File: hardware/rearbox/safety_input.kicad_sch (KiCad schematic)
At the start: 9 parts, among them U9 TLP291-4

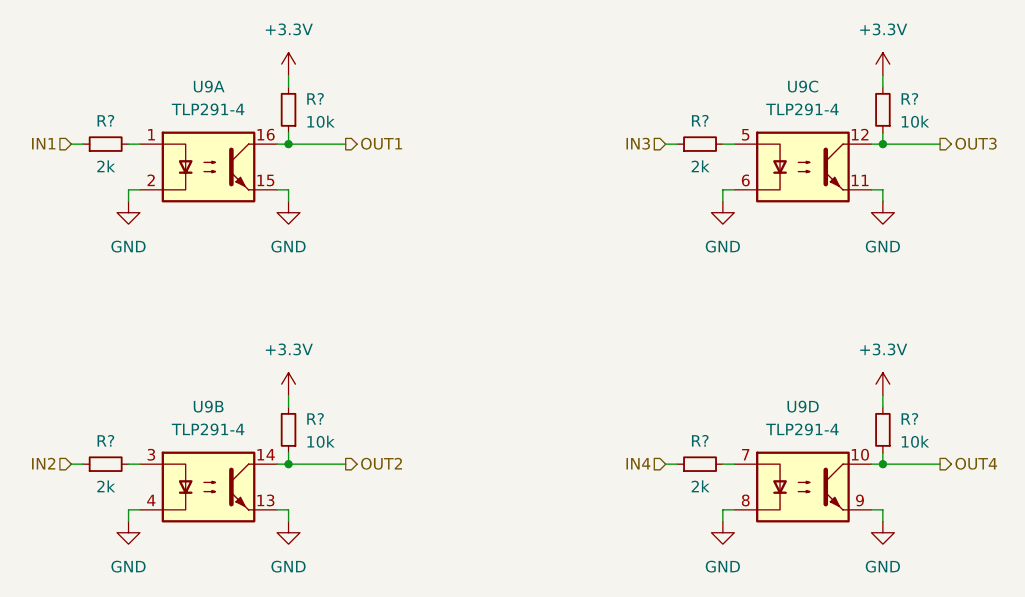
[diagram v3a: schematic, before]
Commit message: Route the tracks on the connector PCB
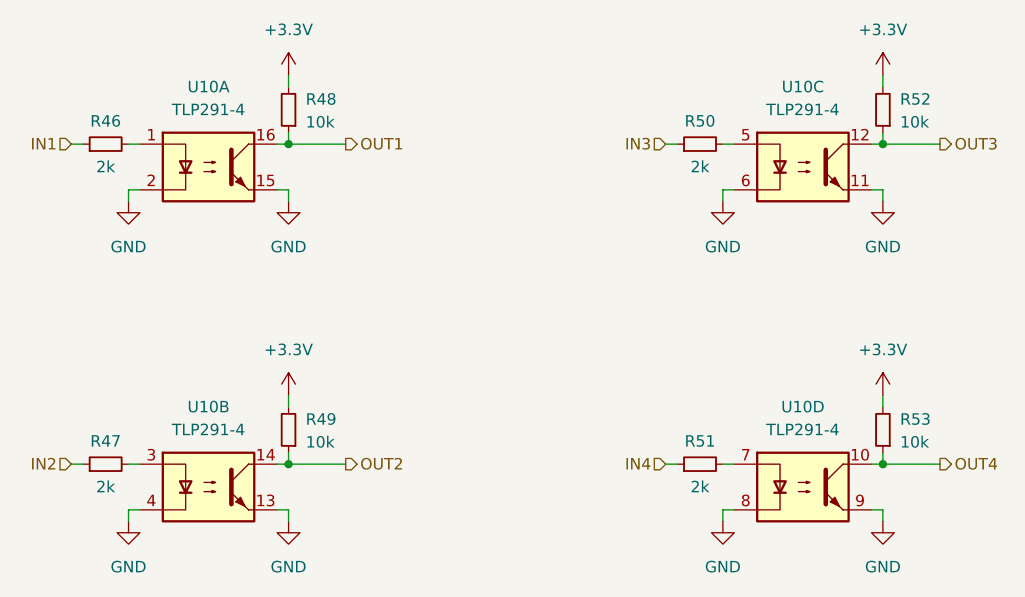
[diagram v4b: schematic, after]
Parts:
- gave numbers to parts that had none: 8
- renumbered U9 to U10

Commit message: Fix measurement bridges polarity
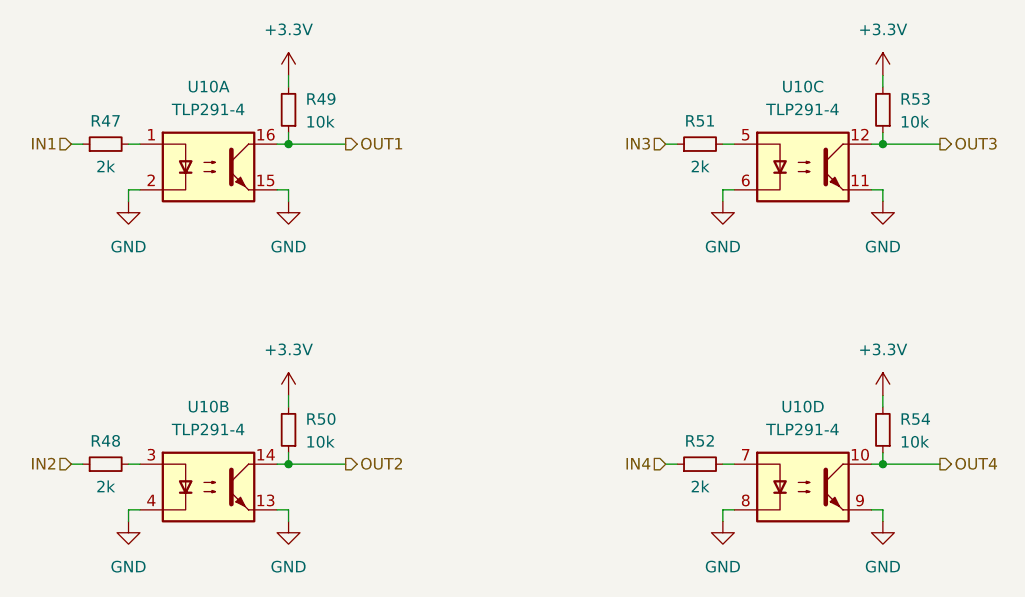
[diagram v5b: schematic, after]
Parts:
- renumbered R46 to R47, R47 to R48, R48 to R49, R49 to R50, R50 to R51, R51 to R52, R52 to R53, R53 to R54

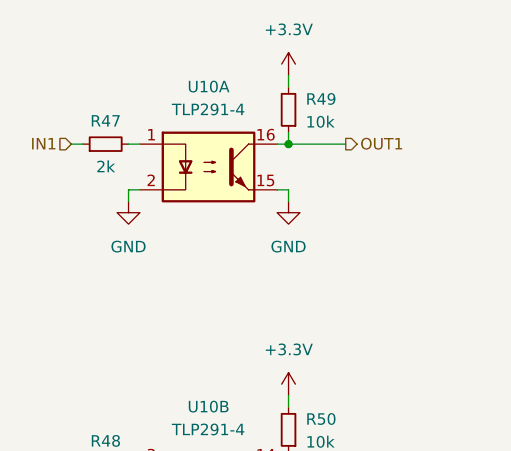
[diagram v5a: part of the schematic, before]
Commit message: Update schematic to reflect hardware changes
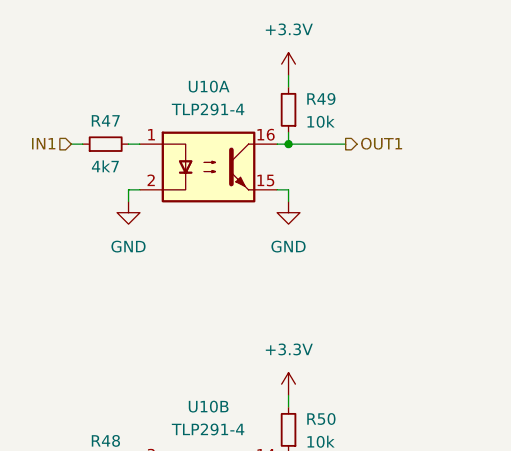
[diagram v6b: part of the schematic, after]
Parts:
- R47: value 2k -> 4k7
